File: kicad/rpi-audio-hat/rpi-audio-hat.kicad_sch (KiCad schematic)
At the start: 10 parts, among them J1 Raspberry_Pi_2_3, J2 Conn_02x20_Counter_Clockwise, J4 Conn_Volume_Slider, J5 Screw_Terminal_01x02, J6 Screw_Terminal_01x02, J7 Screw_Terminal_01x02, SW1 SW_SPDT, U1 PCM5102_breakout, U2 PAM8302A_Adafruit_Board

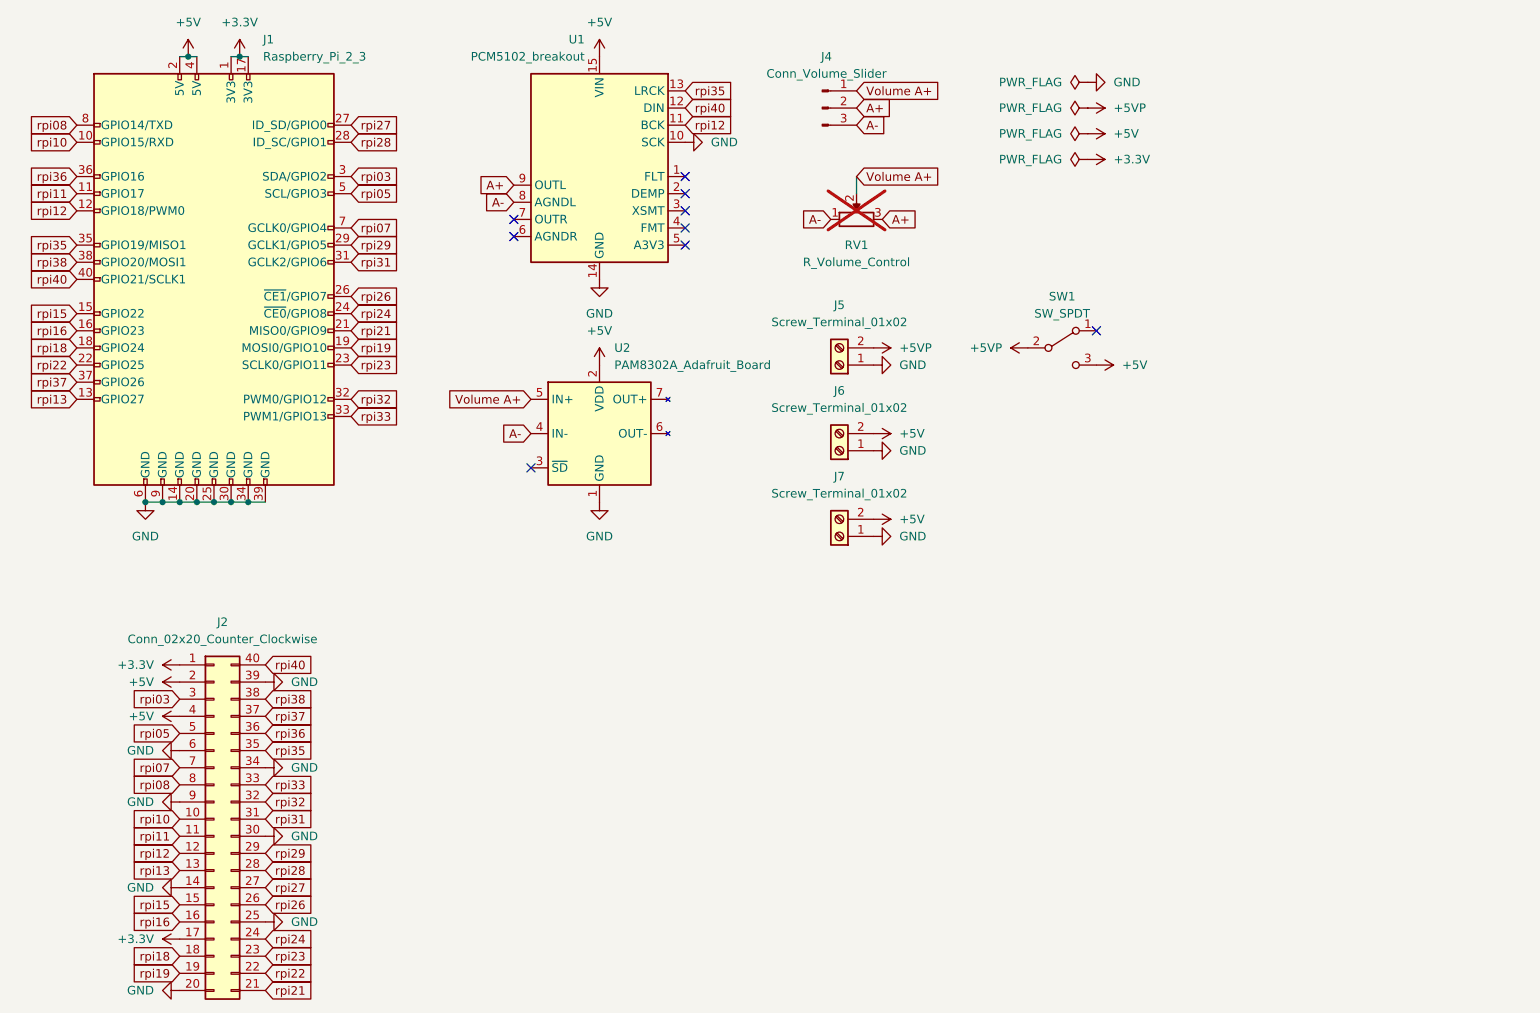
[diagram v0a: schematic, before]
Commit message: rpi-audio-hat: upgrade schematic to KiCad and remove side rows for rpi
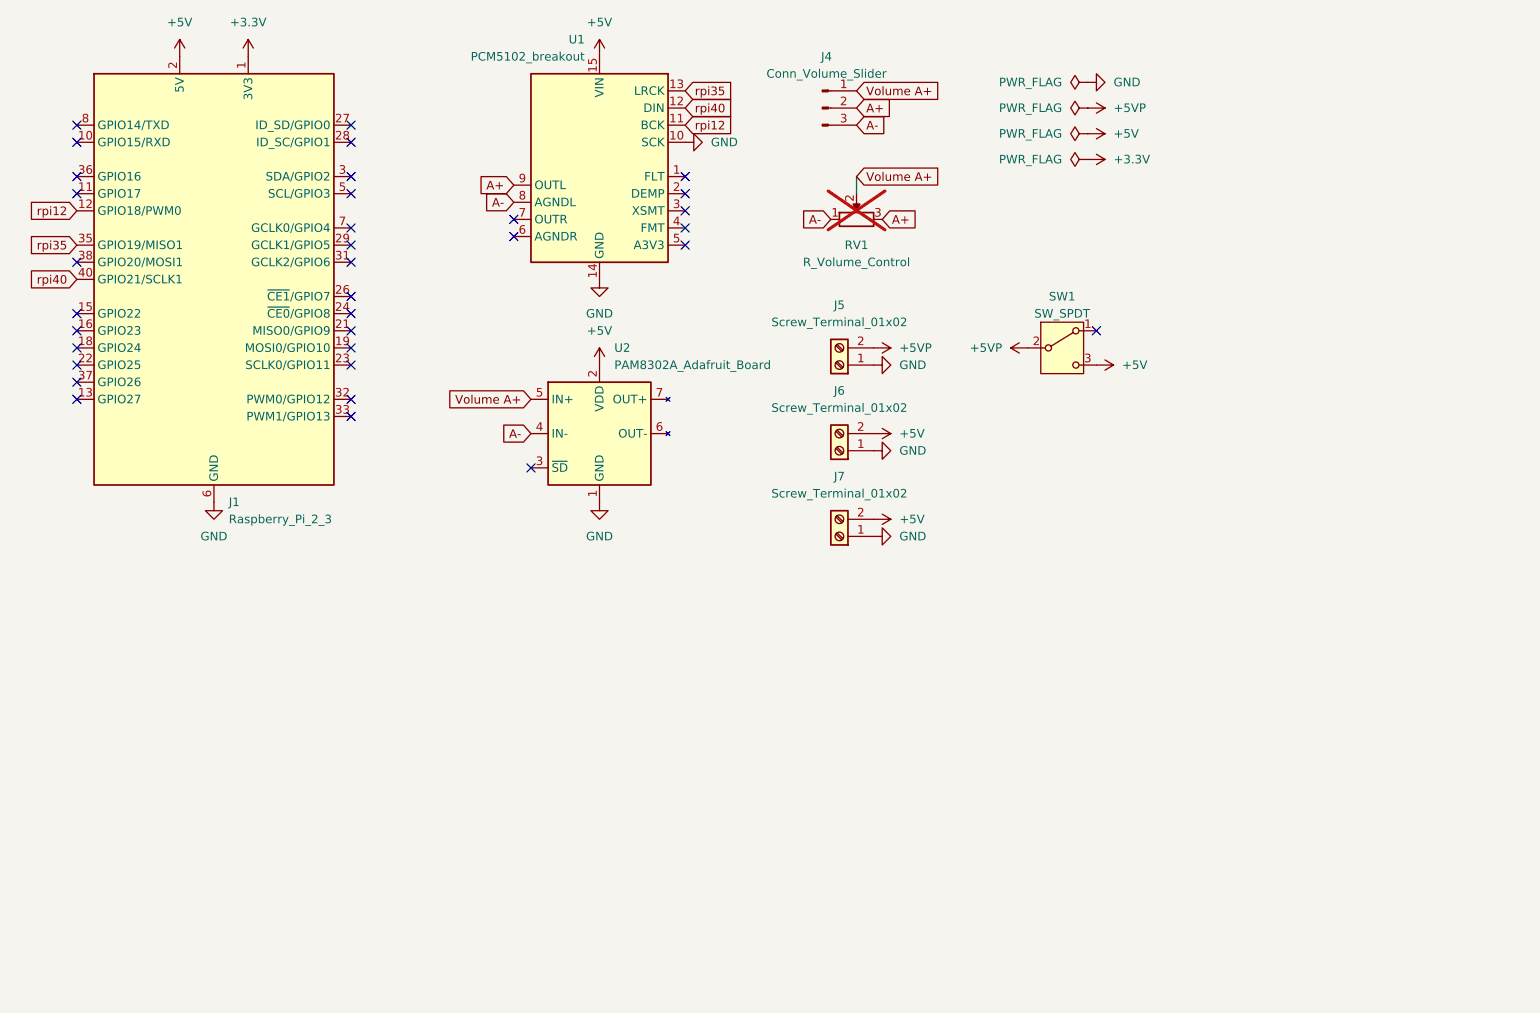
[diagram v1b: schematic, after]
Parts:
- removed J2: Conn_02x20_Counter_Clockwise, Connector_Samtec_HLE_THT:Samtec_HLE-120-02-xx-DV-PE_2x20_P2.54mm_Horizontal, symbol Connector_Generic:Conn_02x20_Counter_Clockwise
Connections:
- net rpi03: no longer names the net of J1.3 (SDA/GPIO2)
- net rpi05: no longer names the net of J1.5 (SCL/GPIO3)
- net rpi07: no longer names the net of J1.7 (GCLK0/GPIO4)
- net rpi08: no longer names the net of J1.8 (GPIO14/TXD)
- net rpi10: no longer names the net of J1.10 (GPIO15/RXD)
- net rpi11: no longer names the net of J1.11 (GPIO17)
- net rpi13: no longer names the net of J1.13 (GPIO27)
- net rpi15: no longer names the net of J1.15 (GPIO22)
- net rpi16: no longer names the net of J1.16 (GPIO23)
- net rpi18: no longer names the net of J1.18 (GPIO24)
- net rpi19: no longer names the net of J1.19 (MOSI0/GPIO10)
- net rpi21: no longer names the net of J1.21 (MISO0/GPIO9)
- net rpi22: no longer names the net of J1.22 (GPIO25)
- net rpi23: no longer names the net of J1.23 (SCLK0/GPIO11)
- net rpi24: no longer names the net of J1.24 (~{CE0}/GPIO8)
- net rpi26: no longer names the net of J1.26 (~{CE1}/GPIO7)
- net rpi27: no longer names the net of J1.27 (ID_SD/GPIO0)
- net rpi28: no longer names the net of J1.28 (ID_SC/GPIO1)
- net rpi29: no longer names the net of J1.29 (GCLK1/GPIO5)
- net rpi31: no longer names the net of J1.31 (GCLK2/GPIO6)
- net rpi32: no longer names the net of J1.32 (PWM0/GPIO12)
- net rpi33: no longer names the net of J1.33 (PWM1/GPIO13)
- net rpi36: no longer names the net of J1.36 (GPIO16)
- net rpi37: no longer names the net of J1.37 (GPIO26)
- net rpi38: no longer names the net of J1.38 (GPIO20/MOSI1)
- no-connect marks 9 -> 34

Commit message: Update PCB for RPi audio hat
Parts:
- U1: footprint Audio_Module:PCM5102_breakout -> MidiatonercaLibrary:PCM5102_breakout
- U2: footprint Audio_Module:PAM8302 -> MidiatonercaLibrary:PAM8302
- renumbered J4 to J2, J5 to J3, J6 to J4, J7 to J5
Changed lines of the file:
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@@
 		(dnp no)
 		(fields_autoplaced yes)
-		(property "Reference" "J5"
+		(property "Reference" "J3"
 			(at 157.48 68.58 0)
 			(effects
@@
 			(project "rpi-audio-hat"
 				(path "/25d551e4-1e32-4b11-b540-b33b7fa395f8"
-					(reference "J5")
+					(reference "J3")
 					(unit 1)
 				)
@@
 		(dnp no)
 		(fields_autoplaced yes)
-		(property "Reference" "J4"
+		(property "Reference" "J2"
 			(at 155.575 31.75 0)
 			(effects
@@
 			(project "rpi-audio-hat"
 				(path "/25d551e4-1e32-4b11-b540-b33b7fa395f8"
-					(reference "J4")
+					(reference "J2")
 					(unit 1)
 				)
@@
 		(dnp no)
 		(fields_autoplaced yes)
-		(property "Reference" "J7"
+		(property "Reference" "J5"
 			(at 157.48 93.98 0)
 			(effects
@@
 			(project "rpi-audio-hat"
 				(path "/25d551e4-1e32-4b11-b540-b33b7fa395f8"
-					(reference "J7")
+					(reference "J5")
 					(unit 1)
 				)
@@
 		(on_board yes)
 		(dnp no)
-		(fields_autoplaced yes)
 		(property "Reference" "U2"
-			(at 124.1141 74.93 0)
+			(at 124.206 97.79 0)
 			(effects
 				(font
@@
 		)
 		(property "Value" "PAM8302A_Adafruit_Board"
-			(at 124.1141 77.47 0)
+			(at 124.206 100.33 0)
 			(effects
 				(font
@@
 			)
 		)
-		(property "Footprint" "Audio_Module:PAM8302"
+		(property "Footprint" "MidiatonercaLibrary:PAM8302"
 			(at 121.92 87.63 0)
 			(effects
@@
 		(dnp no)
 		(fields_autoplaced yes)
-		(property "Reference" "J6"
+		(property "Reference" "J4"
 			(at 157.48 81.28 0)
 			(effects
@@
 			(project "rpi-audio-hat"
 				(path "/25d551e4-1e32-4b11-b540-b33b7fa395f8"
-					(reference "J6")
+					(reference "J4")
 					(unit 1)
 				)
@@
 		(dnp no)
 		(property "Reference" "U1"
-			(at 119.7259 29.21 0)
-			(effects
-				(font
-					(size 1.27 1.27)
-				)
-				(justify left)
+			(at 125.222 64.77 0)
+			(effects
+				(font
+					(size 1.27 1.27)
+				)
+				(justify right)
 			)
 		)
 		(property "Value" "PCM5102_breakout"
-			(at 119.7259 31.75 0)
-			(effects
-				(font
-					(size 1.27 1.27)
-				)
-				(justify left)
-			)
-		)
-		(property "Footprint" "Audio_Module:PCM5102_breakout"
+			(at 124.968 67.31 0)
+			(effects
+				(font
+					(size 1.27 1.27)
+				)
+				(justify right)
+			)
+		)
+		(property "Footprint" "MidiatonercaLibrary:PCM5102_breakout"
 			(at 123.19 27.94 0)
 			(effects

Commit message: Work on schematic
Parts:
- added RV2, RV3: R_Volume_Control, symbol Device:R_Potentiometer
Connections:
- net GND: now also RV2.3, RV3.3
- new net DAC/DAC-L: RV2.1
- new net DAC/DAC-R: RV3.1
- new net Stereo amplifier/IN-L: RV2.2
- new net Stereo amplifier/IN-R: RV3.2
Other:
- added sheet Battery charger (Battery charger.kicad_sch)
- added sheet DAC (DAC.kicad_sch)
- added sheet Power (Power.kicad_sch)
- added sheet Stereo amplifier (Stereo amplifier.kicad_sch)
- moved on the sheet: J5

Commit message: Fix power switch & symbol update
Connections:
- net +5V: no longer SW1.3 (C)
- net +5VP: no longer SW1.2 (B)
- new net +VBAT: SW1.2 (B)
- new net +VBAT-SW: SW1.3 (C)
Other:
- note added: "Power switch"
- note added: "Switches on every power consumer"
- moved on the sheet: SW1
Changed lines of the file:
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@@
 	)
 	(no_connect
-		(at 195.58 72.39)
+		(at 242.57 115.57)
 	)
 	(no_connect
@@
 	(wire
 		(pts
-			(xy 147.32 116.84) (xy 147.32 114.3)
+			(xy 242.57 120.65) (xy 250.19 120.65)
 		)
 		(stroke
@@
 	(wire
 		(pts
-			(xy 160.02 49.53) (xy 160.02 52.07)
+			(xy 147.32 116.84) (xy 147.32 114.3)
 		)
 		(stroke
@@
 	(wire
 		(pts
-			(xy 140.97 127) (xy 140.97 119.38)
+			(xy 160.02 49.53) (xy 160.02 52.07)
 		)
 		(stroke
@@
 	(wire
 		(pts
-			(xy 171.45 120.65) (xy 166.37 120.65)
+			(xy 140.97 127) (xy 140.97 119.38)
 		)
 		(stroke
@@
 	(wire
 		(pts
-			(xy 140.97 119.38) (xy 123.19 119.38)
+			(xy 224.79 118.11) (xy 232.41 118.11)
 		)
 		(stroke
@@
 	(wire
 		(pts
-			(xy 123.19 116.84) (xy 147.32 116.84)
+			(xy 171.45 120.65) (xy 166.37 120.65)
 		)
 		(stroke
@@
 	(wire
 		(pts
-			(xy 147.32 114.3) (xy 153.67 114.3)
+			(xy 140.97 119.38) (xy 123.19 119.38)
 		)
 		(stroke
@@
 		)
 	)
+	(wire
+		(pts
+			(xy 123.19 116.84) (xy 147.32 116.84)
+		)
+		(stroke
+			(width 0)
+			(type default)
+		)
+	)
+	(wire
+		(pts
+			(xy 250.19 119.38) (xy 250.19 120.65)
+		)
+		(stroke
+			(width 0)
+			(type default)
+		)
+	)
+	(wire
+		(pts
+			(xy 224.79 111.76) (xy 224.79 118.11)
+		)
+		(stroke
+			(width 0)
+			(type default)
+		)
+	)
+	(wire
+		(pts
+			(xy 147.32 114.3) (xy 153.67 114.3)
+		)
+		(stroke
+			(width 0)
+			(type default)
+		)
+	)
+	(rectangle
+		(start 218.44 91.44)
+		(end 259.08 127)
+		(stroke
+			(width 0)
+			(type dash)
+		)
+		(fill
+			(type none)
+		)
+	)
+	(text "Switches on every power consumer"
+		(exclude_from_sim no)
+		(at 239.522 99.568 0)
+		(effects
+			(font
+				(size 1.27 1.27)
+			)
+		)
+	)
+	(text "Power switch"
+		(exclude_from_sim no)
+		(at 239.268 95.758 0)
+		(effects
+			(font
+				(size 3 3)
+			)
+		)
+	)
 	(global_label "A-"
 		(shape input)
@@
 	)
 	(symbol
-		(lib_id "power:+5V")
-		(at 195.58 77.47 270)
-		(unit 1)
-		(exclude_from_sim no)
-		(in_bom yes)
-		(on_board yes)
-		(dnp no)
-		(fields_autoplaced yes)
-		(property "Reference" "#PWR0113"
-			(at 191.77 77.47 0)
-			(effects
-				(font
-					(size 1.27 1.27)
-				)
-				(hide yes)
-			)
-		)
-		(property "Value" "+5V"
-			(at 199.39 77.47 90)
-			(effects
-				(font
-					(size 1.27 1.27)
-				)
-				(justify left)
-			)
-		)
-		(property "Footprint" ""
-			(at 195.58 77.47 0)
-			(effects
-				(font
-					(size 1.27 1.27)
-				)
-				(hide yes)
-			)
-		)
-		(property "Datasheet" ""
-			(at 195.58 77.47 0)
-			(effects
-				(font
-					(size 1.27 1.27)
-				)
-				(hide yes)
-			)
-		)
-		(property "Description" "Power symbol creates a global label with name \"+5V\""
-			(at 195.58 77.47 0)
-			(effects
-				(font
-					(size 1.27 1.27)
-				)
-				(hide yes)
-			)
-		)
-		(pin "1"
-		)
-		(instances
-			(project "rpi-audio-hat"
-				(path "/25d551e4-1e32-4b11-b540-b33b7fa395f8"
-					(reference "#PWR0113")
-					(unit 1)
-				)
-			)
-		)
-	)
-	(symbol
 		(lib_id "power:GND")
 		(at 121.92 64.77 0)
@@
 	)
 	(symbol
+		(lib_id "power:+5V")
+		(at 224.79 111.76 0)
+		(unit 1)
+		(exclude_from_sim no)
+		(in_bom yes)
+		(on_board yes)
+		(dnp no)
+		(fields_autoplaced yes)
+		(property "Reference" "#PWR061"
+			(at 224.79 115.57 0)
+			(effects
+				(font
+					(size 1.27 1.27)
+				)
+				(hide yes)
+			)
+		)
+		(property "Value" "+VBAT"
+			(at 224.79 106.68 0)
+			(effects
+				(font
+					(size 1.27 1.27)
+				)
+			)
+		)
+		(property "Footprint" ""
+			(at 224.79 111.76 0)
+			(effects
+				(font
+					(size 1.27 1.27)
+				)
+				(hide yes)
+			)
+		)
+		(property "Datasheet" ""
+			(at 224.79 111.76 0)
+			(effects
+				(font
+					(size 1.27 1.27)
+				)
+				(hide yes)
+			)
+		)
+		(property "Description" ""
+			(at 224.79 111.76 0)
+			(effects
+				(font
+					(size 1.27 1.27)
+				)
+				(hide yes)
+			)
+		)
+		(pin "1"
+		)
+		(instances
+			(project "rpi-audio-hat"
+				(path "/25d551e4-1e32-4b11-b540-b33b7fa395f8"
+					(reference "#PWR061")
+					(unit 1)
+				)
+			)
+		)
+	)
+	(symbol
 		(lib_id "power:+3.3V")
 		(at 194.31 46.99 270)
@@
 	(symbol
 		(lib_id "power:+5V")
+		(at 250.19 119.38 0)
+		(unit 1)
+		(exclude_from_sim no)
+		(in_bom yes)
+		(on_board yes)
+		(dnp no)
+		(fields_autoplaced yes)
+		(property "Reference" "#PWR062"
+			(at 250.19 123.19 0)
+			(effects
+				(font
+					(size 1.27 1.27)
+				)
+				(hide yes)
+			)
+		)
+		(property "Value" "+VBAT-SW"
+			(at 250.19 114.3 0)
+			(effects
+				(font
+					(size 1.27 1.27)
+				)
+			)
+		)
+		(property "Footprint" ""
+			(at 250.19 119.38 0)
+			(effects
+				(font
+					(size 1.27 1.27)
+				)
+				(hide yes)
+			)
+		)
+		(property "Datasheet" ""
+			(at 250.19 119.38 0)
+			(effects
+				(font
+					(size 1.27 1.27)
+				)
+				(hide yes)
+			)
+		)
+		(property "Description" ""
+			(at 250.19 119.38 0)
+			(effects
+				(font
+					(size 1.27 1.27)
+				)
+				(hide yes)
+			)
+		)
+		(pin "1"
+		)
+		(instances
+			(project "rpi-audio-hat"
+				(path "/25d551e4-1e32-4b11-b540-b33b7fa395f8"
+					(reference "#PWR062")
+					(unit 1)
+				)
+			)
+		)
+	)
+	(symbol
+		(lib_id "power:+5V")
 		(at 59.69 31.75 0)
 		(unit 1)
@@
 	)
 	(symbol
-		(lib_id "power:+5VP")
-		(at 185.42 74.93 90)
-		(unit 1)
-		(exclude_from_sim no)
-		(in_bom yes)
-		(on_board yes)
-		(dnp no)
-		(fields_autoplaced yes)
-		(property "Reference" "#PWR0101"
-			(at 189.23 74.93 0)
-			(effects
-				(font
-					(size 1.27 1.27)
-				)
-				(hide yes)
-			)
-		)
-		(property "Value" "+5VP"
-			(at 181.61 74.93 90)
-			(effects
-				(font
-					(size 1.27 1.27)
-				)
-				(justify left)
-			)
-		)
-		(property "Footprint" ""
-			(at 185.42 74.93 0)
-			(effects
-				(font
-					(size 1.27 1.27)
-				)
-				(hide yes)
-			)
-		)
-		(property "Datasheet" ""
-			(at 185.42 74.93 0)
-			(effects
-				(font
-					(size 1.27 1.27)
-				)
-				(hide yes)
-			)
-		)
-		(property "Description" "Power symbol creates a global label with name \"+5VP\""
-			(at 185.42 74.93 0)
-			(effects
-				(font
-					(size 1.27 1.27)
-				)
-				(hide yes)
-			)
-		)
-		(pin "1"
-		)
-		(instances
-			(project "rpi-audio-hat"
-				(path "/25d551e4-1e32-4b11-b540-b33b7fa395f8"
-					(reference "#PWR0101")
-					(unit 1)
-				)
-			)
-		)
-	)
-	(symbol
 		(lib_id "Switch:SW_SPDT")
-		(at 190.5 74.93 0)
+		(at 237.49 118.11 0)
 		(unit 1)
 		(exclude_from_sim no)
@@
 		(fields_autoplaced yes)
 		(property "Reference" "SW1"
-			(at 190.5 67.31 0)
+			(at 237.49 110.49 0)
 			(effects
 				(font
@@
 		)
 		(property "Value" "SW_SPDT"
-			(at 190.5 69.85 0)
+			(at 237.49 113.03 0)
 			(effects
 				(font
@@
 		)
 		(property "Footprint" "MidiatonercaLibrary:SW_3P_Mini_Toggle_B068BW_SPDT"
-			(at 190.5 74.93 0)
+			(at 237.49 118.11 0)
 			(effects
 				(font
@@
 		)
 		(property "Datasheet" "~"
-			(at 190.5 74.93 0)
+			(at 237.49 118.11 0)
 			(effects
 				(font
@@
 		)
 		(property "Description" "Switch, single pole double throw"
-			(at 190.5 74.93 0)
-			(effects
-				(font
+			(at 237.49 118.11 0)
+			(effects
+				(font
